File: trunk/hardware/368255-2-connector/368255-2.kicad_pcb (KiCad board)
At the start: 2 copper layers, 145.4 x 59.7 mm, 38 parts, among them P1 368255-2, P10 CONN_1, P11 CONN_1, P12 CONN_1, P13 CONN_1, P14 CONN_1, P15 CONN_1, P16 CONN_1, P17 CONN_1, P18 CONN_1, P19 CONN_1, P2 CONN_19, P20 CONN_1, P21 CONN_1, P22 CONN_1, P23 CONN_1, P24 CONN_1, P25 CONN_1, P26 CONN_1, P27 CONN_1, P28 CONN_1, P29 CONN_1, P3 CONN_19, P30 CONN_1, P31 CONN_1, P32 CONN_8, P33 CONN_8, P34 CONN_8, P35 CONN_8, P4 CONN_19, P5 CONN_19, P6 CONN_1, P7 CONN_1, P8 CONN_1, P9 CONN_1

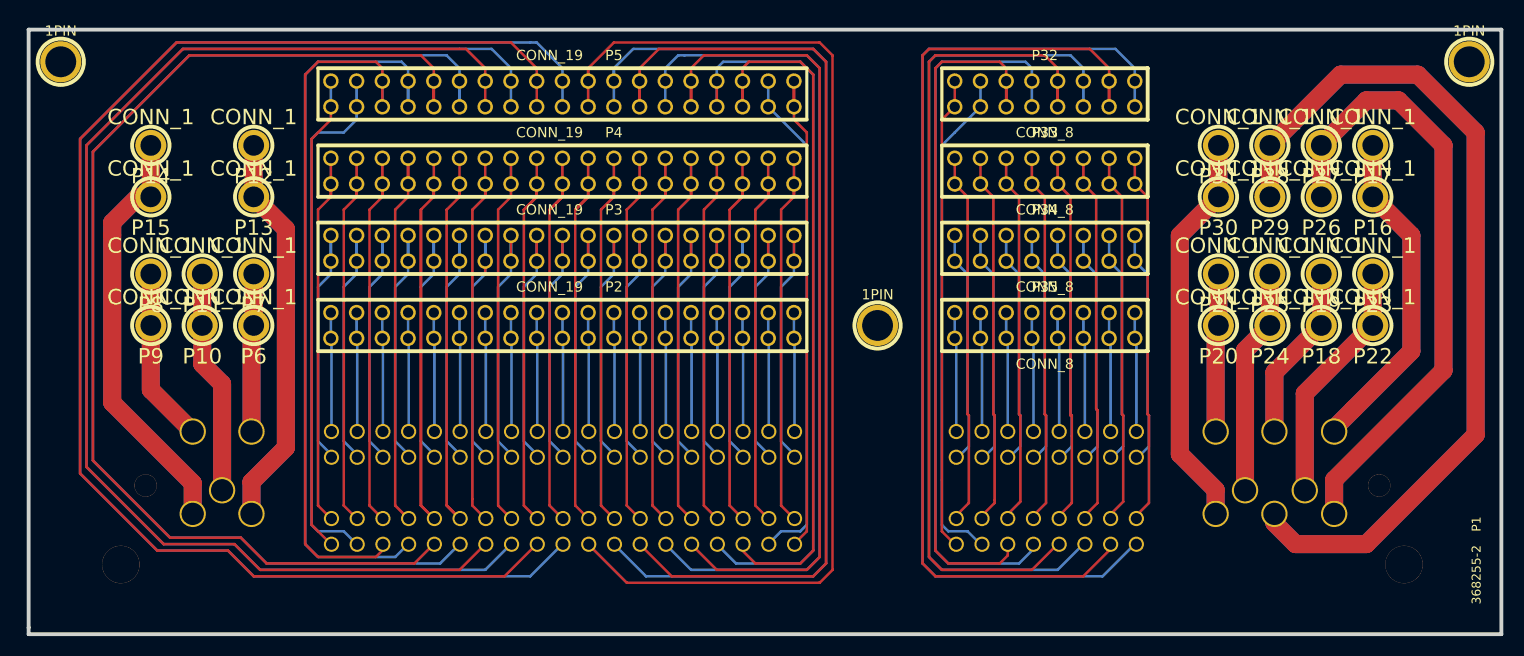
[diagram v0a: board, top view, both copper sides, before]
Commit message: 
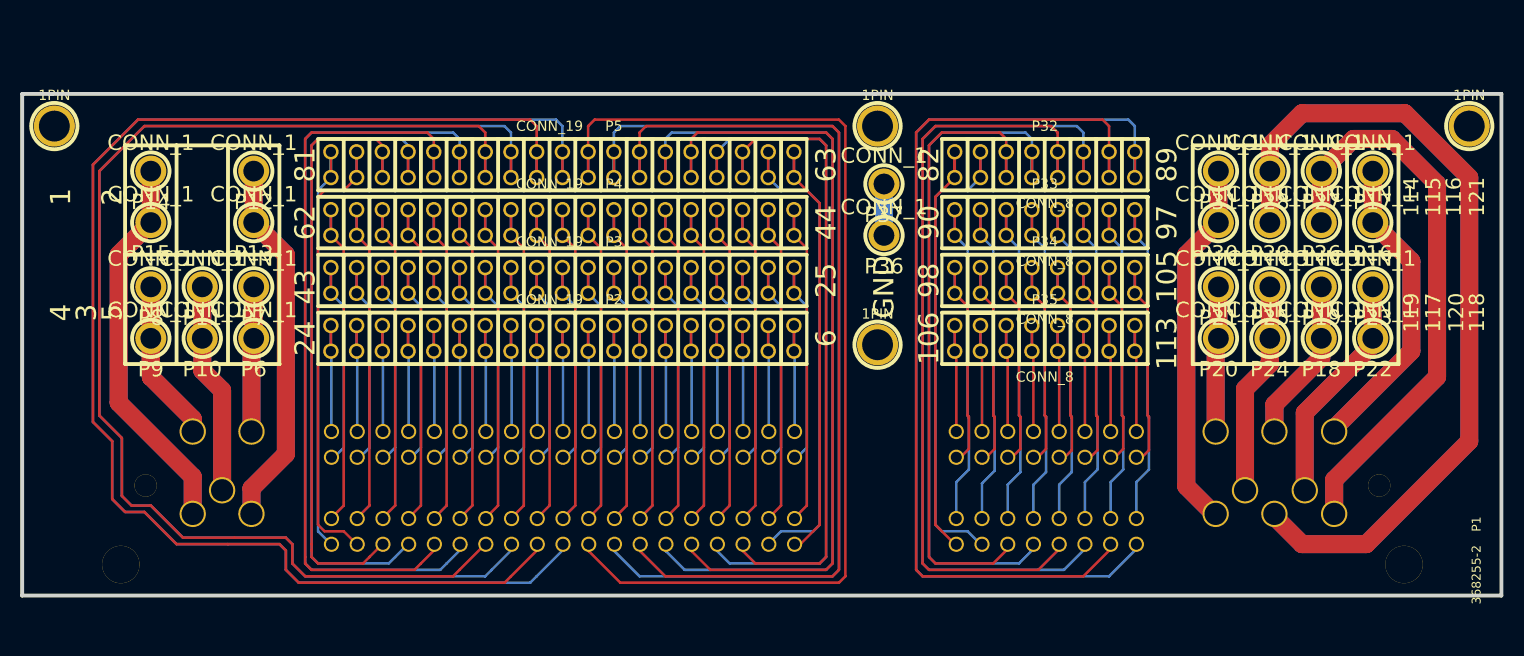
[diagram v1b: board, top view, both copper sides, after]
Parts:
- removed the 1PIN at (58.4, 55.2)
- removed the 1PIN at (197.5, 55.2)
- removed the 1PIN at (139.1, 81.3)
- added 1PIN: P***, 1pin, F.Cu at (57.8, 61.6)
- added 1PIN: P***, 1pin, F.Cu at (139.1, 61.6)
- added 1PIN: P***, 1pin, F.Cu at (197.5, 61.6)
- added 1PIN: P***, 1pin, F.Cu at (139.1, 83.2)
- added P36: CONN_1, 1pin(m), F.Cu at (139.7, 72.4)
- added P37: CONN_1, 1pin(m), F.Cu at (139.7, 67.3)
- moved P32 6.98 mm to (155.6, 65.4)
- moved P5 6.98 mm to (106.7, 65.4)
- moved P33 5.08 mm to (155.6, 71.1)
- moved P4 5.08 mm to (106.7, 71.1)
- moved P3 3.17 mm to (106.7, 76.8)
- moved P34 3.17 mm to (155.6, 76.8)
- moved P12 2.54 mm to (77.5, 66.0)
- moved P13 2.54 mm to (77.5, 71.1)
- moved P14 2.54 mm to (67.3, 66.0)
- moved P15 2.54 mm to (67.3, 71.1)
- moved P16 2.54 mm to (188.0, 71.1)
- moved P17 2.54 mm to (188.0, 66.0)
- moved P26 2.54 mm to (182.9, 71.1)
- moved P27 2.54 mm to (182.9, 66.0)
- moved P28 2.54 mm to (177.8, 66.0)
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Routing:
- net N-00000103: track 113.7 -> 75.9 mm
- net N-00000104: track 118.7 -> 83.5 mm
- net N-0000030: track 69.0 -> 34.1 mm
- net GND: track 0.00 -> 15.2 mm
- net N-0000086: track 123.4 -> 112.9 mm
- net N-00000101: track 70.2 -> 62.0 mm
- net N-00000102: track 74.9 -> 67.0 mm
- net N-00000122: track 84.0 -> 76.4 mm
- net N-0000076: track 70.6 -> 64.5 mm
- net N-0000088: track 78.9 -> 72.9 mm
- net N-00000100: track 52.4 -> 46.7 mm
- net N-0000031: track 39.8 -> 34.1 mm
- net N-0000035: track 39.7 -> 34.1 mm
- net N-0000036: track 39.7 -> 34.1 mm
- net N-0000034: track 39.7 -> 34.1 mm
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- added copper zone on B.Cu, net GND
- added copper zone on F.Cu, net GND
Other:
- board size 145.4 x 59.7 mm -> 146.1 x 49.5 mm
- board text added: "1"
- board text added: "105"
- board text added: "106"
- board text added: "113"
- board text added: "114"
- board text added: "115"
- board text added: "116"
- board text added: "117"
- board text added: "118"
- board text added: "119"
- board text added: "120"
- board text added: "121"
- board text added: "2"
- board text added: "24"
- board text added: "25"
- board text added: "3"
- board text added: "4"
- board text added: "43"
- board text added: "44"
- board text added: "5"
- board text added: "6"
- board text added: "62"
- board text added: "63"
- board text added: "81"
- board text added: "82"
- board text added: "89"
- board text added: "90"
- board text added: "97"
- board text added: "98"
- board text added: "GND"
